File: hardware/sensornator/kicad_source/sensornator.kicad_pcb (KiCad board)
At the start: 2 copper layers, 78 x 53 mm, 50 parts, among them CN1 ARDUINO, CON1 Micro_SDCard, P1 USB_OTG, Q1 2N7002, Q2 2N7002, SW1 TAST_VER, SW2 TAST_VER, U1 TPS383X, U2 MCP73831, U3 TPS736XX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

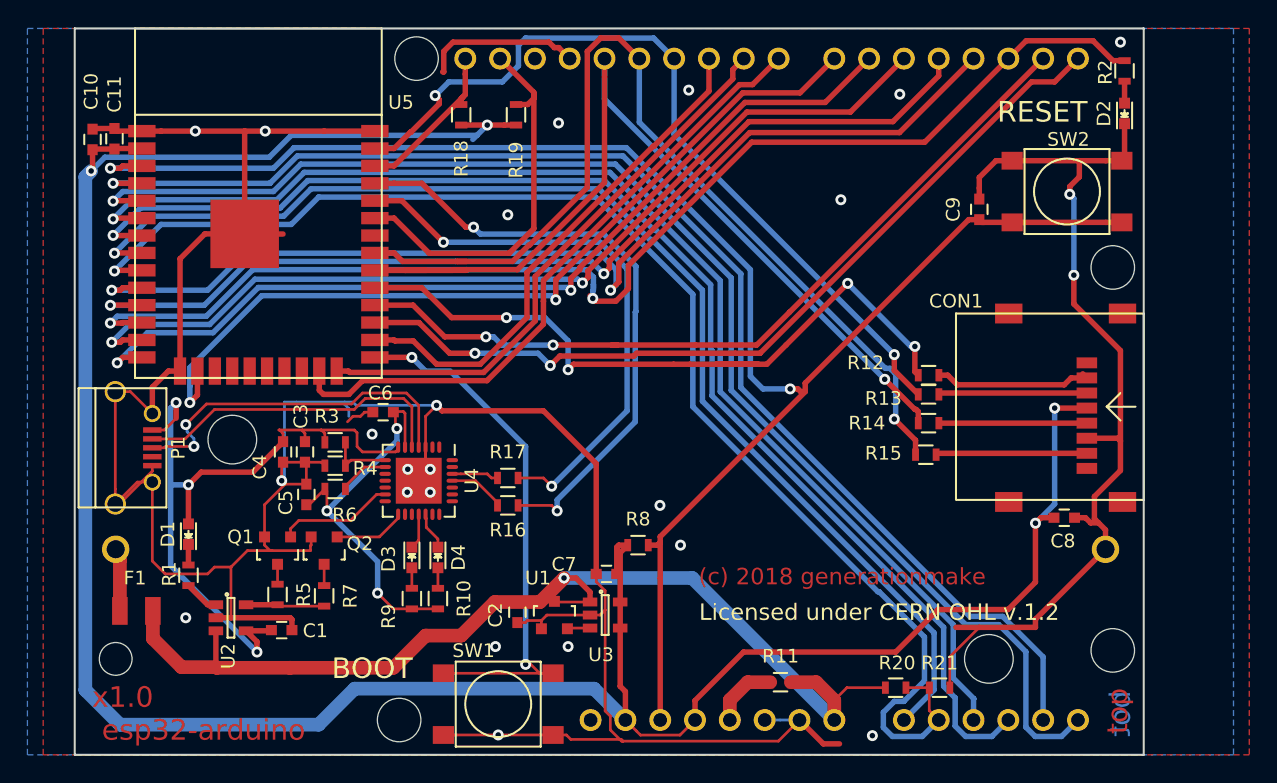
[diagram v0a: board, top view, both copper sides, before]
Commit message: updated schematic, added extra pages for history and usb, added esp32 reset circuit
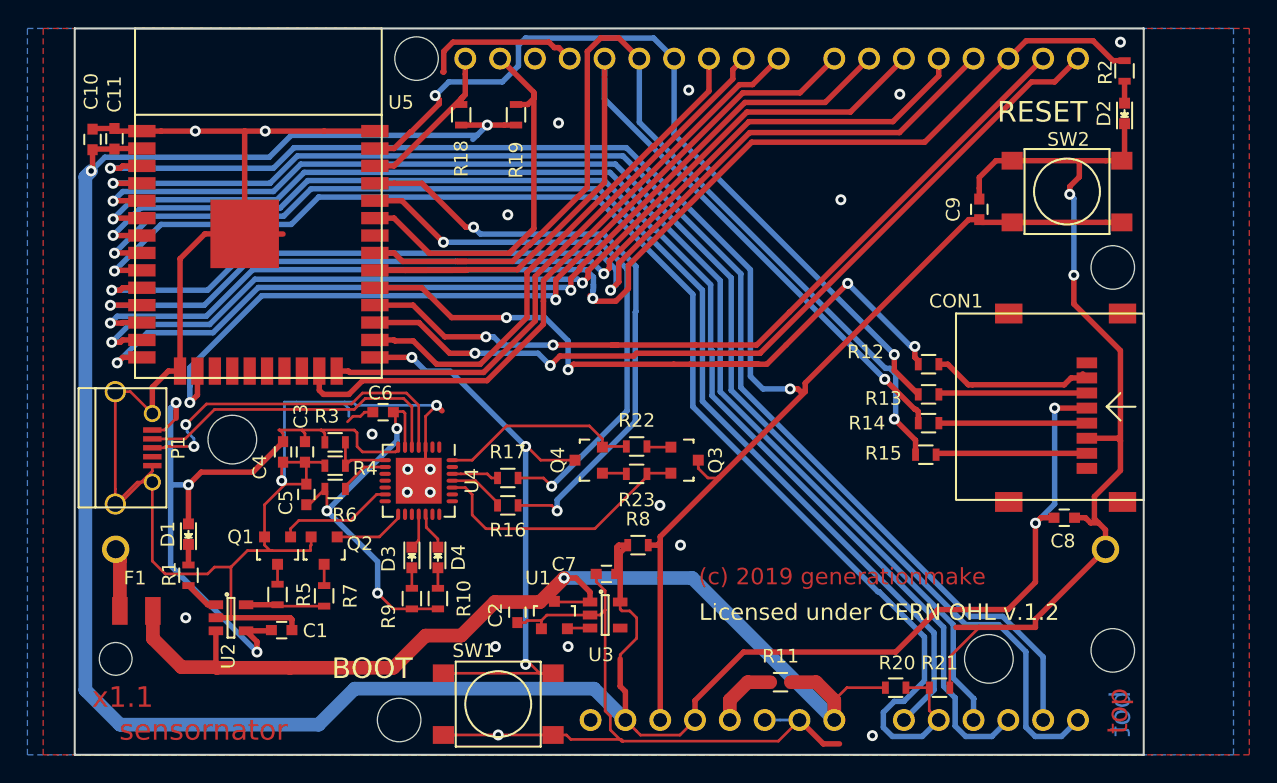
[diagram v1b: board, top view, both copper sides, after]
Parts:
- added Q3: BC847, SOT_TO:SOT-23, F.Cu at (89.5, 108.5)
- added Q4: BC847, SOT_TO:SOT-23, F.Cu at (82.5, 108.5)
- added R22: 10k, resistors:R_0603, F.Cu at (86.0, 107.5)
- added R23: 10k, resistors:R_0603, F.Cu at (86.0, 109.5)
- D1: value green -> yellow
- D2: value green -> blue
- D4: value green -> red
- R1: value 1k -> 4k7
- moved R12 0.80 mm to (107.3, 101.5)
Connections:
- net /BOOT renamed BOOT
- net /CHR_100MA renamed /USB and Power/CHR_100MA
- net /CHR_500MA renamed /USB and Power/CHR_500MA
- net /PROG renamed /USB and Power/PROG
- net /RESET renamed RESET
- net /RX renamed RX
- net /RX_R renamed /USB and Power/RX_R
- net /TX renamed TX
- net /TX_R renamed /USB and Power/TX_R
- U3 pad 4: +3V3 -> (no net)
- U4 pad 24: (no net) -> /USB and Power/RTS
- U4 pad 28: (no net) -> /USB and Power/DTR
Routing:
- net GND: track 305.0 -> 284.1 mm
- net /USB and Power/RTS: track 0.00 -> 19.9 mm
- net /USB and Power/DTR: track 0.00 -> 14.7 mm
- net BOOT: track 39.9 -> 43.9 mm, vias 2 -> 3
- net RESET: track 123.7 -> 126.1 mm
- net /USB and Power/RTS_R: track 0.00 -> 1.77 mm
- net /USB and Power/DTR_R: track 0.00 -> 1.77 mm
- net +3V3: track 192.1 -> 193.4 mm
- net /SPI_CS_SD: track 52.9 -> 52.1 mm
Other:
- board text added: "(c) 2019 generationmake"
- board text added: "sensornator"
- board text added: "x1.1"
- board text removed: "(c) 2018 generationmake"
- board text removed: "esp32-arduino"
- board text removed: "x1.0"

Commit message: changed micro SD card socket to push pull type, updated footprint of micro USB socket
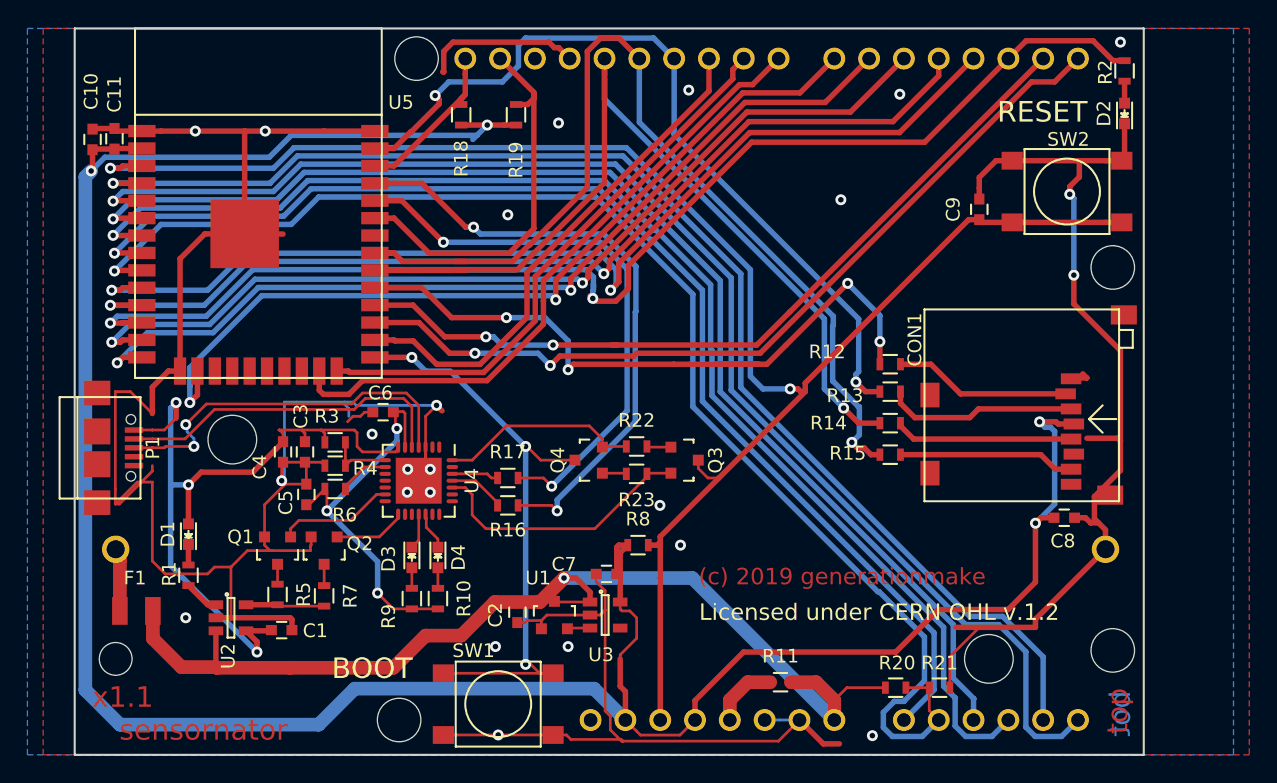
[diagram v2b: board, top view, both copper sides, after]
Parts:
- CON1: footprint CON_wuerth:WE_693072010801 -> CON_wuerth:WE_693071010811
- P1: footprint mechanical-connectors:USB_Micro-B -> CON_wuerth:WE_629105136821
- moved CON1 7.27 mm to (107.0, 111.5)
- moved R13 2.81 mm to (104.5, 103.5)
- moved R12 2.80 mm to (104.5, 101.5)
- moved R14 2.80 mm to (104.5, 105.8)
- moved R15 2.60 mm to (104.5, 108.1)
- moved P1 0.90 mm to (50.0, 107.6)
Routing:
- net /SPI_MOSI_R: track 10.8 -> 14.0 mm
- net /SPI_CLK_R: track 10.8 -> 13.0 mm
- net /SPI_MISO_R: track 11.0 -> 12.9 mm
- net (no net): track 0.00 -> 1.57 mm
- net VIN: track 53.5 -> 54.8 mm
- net Net-(P1-Pad2): track 23.4 -> 24.7 mm
- net Net-(P1-Pad3): track 26.3 -> 27.6 mm
- net /SPI_CS_SD: track 52.1 -> 50.8 mm
- net /SPI_CS_SD_R: track 12.1 -> 12.9 mm
- net /SPI_MOSI: track 59.3 -> 58.8 mm

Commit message: updated schematic, added USB voltage bypass, finished layout, corrected 3D models
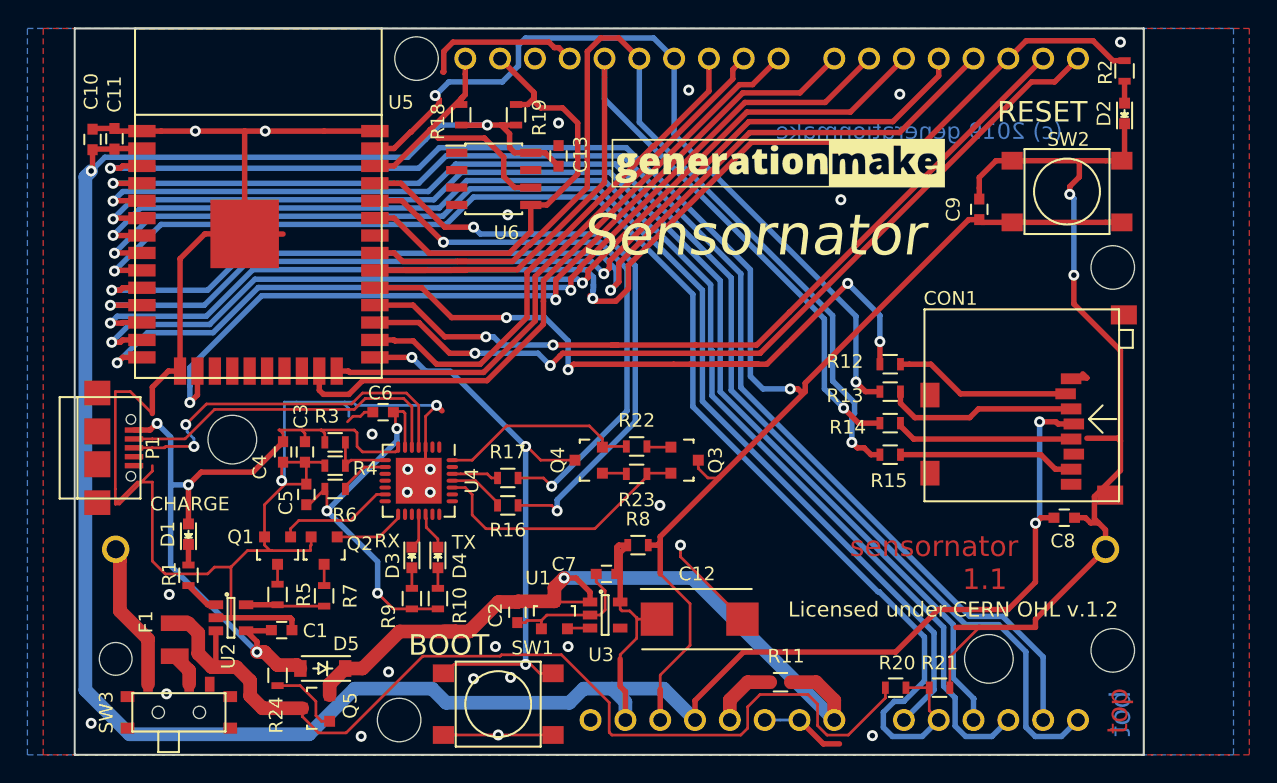
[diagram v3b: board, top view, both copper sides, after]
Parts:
- added C12: 100u/6.3V, capacitors:TantalC_SizeD_EIA-7343_Reflow, F.Cu at (90.6, 120.1)
- added C13: 100n, capacitors:C_0603, F.Cu at (80.3, 86.3)
- added D5: MBR120, diodes:SOD-123, F.Cu at (63.1, 123.7)
- added G***: generationmake_logo, labels:generationmake_logo, F.Cu at (96.3, 92.1)
- added Q5: NTR4171P, SOT_TO:SOT-23, F.Cu at (62.6, 126.6)
- added R24: 4k7, resistors:R_0603, F.Cu at (59.8, 124.2)
- added SW3: SWITCH_INV, mechanical-switches:WE_450404015514, F.Cu at (52.6, 126.9)
- added U6: ATECC608A, SOIC:SOIC-8_3.9x4.9mm_Pitch1.27mm, F.Cu at (75.6, 88.0)
- moved F1 3.50 mm to (52.3, 121.6), turned to 270 degrees
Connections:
- C2 pad 1: +BATT -> VCC
- CN1 pad 24: +BATT -> VCC
- F1 pad 2: Net-(BT1-Pad1) -> Net-(F1-Pad2)
- R11 pad 2: +BATT -> VCC
- U1 pad 3: +BATT -> VCC
- U3 pad 1: +BATT -> VCC
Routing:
- net VCC: track 0.00 -> 60.7 mm, vias 0 -> 1
- net GND: track 284.1 -> 262.4 mm, vias 24 -> 29
- net +BATT: track 81.9 -> 71.9 mm, vias 1 -> 0
- net /I2C_SCL: track 12.0 -> 21.9 mm
- net +3V3: track 193.3 -> 202.5 mm
- net Net-(BT1-Pad1): track 3.70 -> 9.90 mm
- net Net-(Q5-Pad1): track 0.00 -> 5.49 mm
- net /I2C_SDA: track 28.6 -> 32.9 mm
- net Net-(F1-Pad2): track 0.00 -> 2.48 mm
- net RESET: track 126.1 -> 127.9 mm
- net BOOT: track 43.9 -> 42.1 mm
- net (no net): vias 0 -> 1
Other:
- board text added: "1.1"
- board text added: "CHARGE"
- board text added: "RX"
- board text added: "Sensornator"
- board text added: "TX"
- board text removed: "x1.1"

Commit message: added silk screen on back side, updated parameters, generated pdf schematic
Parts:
- added G***: generationmake_logo, labels:generationmake_logo, B.Cu at (61.7, 93.5)
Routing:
- net GND: track 262.4 -> 290.7 mm
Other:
- board text added: "(c) 2019"
- board text added: "3.3V/3.0V"
- board text added: "5V/VBAT"
- board text added: "A0/IO32"
- board text added: "A1/IO33/VBAT"
- board text added: "A2/IO34"
- board text added: "A3/IO35"
- board text added: "A4/IO36"
- board text added: "A5/IO39"
- board text added: "AREF/NC"
- board text added: "D0/RX/IO16"
- board text added: "D1/TX/IO17"
- board text added: "D10/CS/IO4"
- board text added: "D11/MOSI/IO23"
- board text added: "D12/MISO/IO19"
- board text added: "D13/CLK/IO16"
- board text added: "D2/IO27"
- board text added: "D3/DAC1/IO25"
- board text added: "D4/DAC2/IO26"
- board text added: "D5/IO14"
- board text added: "D6/IO12"
- board text added: "D7/IO13"
- board text added: "D8/IO15"
- board text added: "D9/IO2"
- board text added: "GND"
- board text added: "IOREF/3.0V"
- board text added: "SCL"
- board text added: "SDA"
- board text added: "VIN/VBAT"
- board text added: "generationmake"
- board text added: "nc"
- board text removed: "(c) 2019 generationmake"
